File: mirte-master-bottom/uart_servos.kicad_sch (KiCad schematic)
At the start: 7 parts, among them J14 servo_connector, J17 servo_connector_small

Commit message: upd main layout v3
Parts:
- JP1: value LED_POWER_SELECT -> SERVO_POWER_SELECT
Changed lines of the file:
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@@
 			)
 		)
-		(property "Value" "LED_POWER_SELECT"
+		(property "Value" "SERVO_POWER_SELECT"
 			(at 76.2 91.44 90)
 			(effects

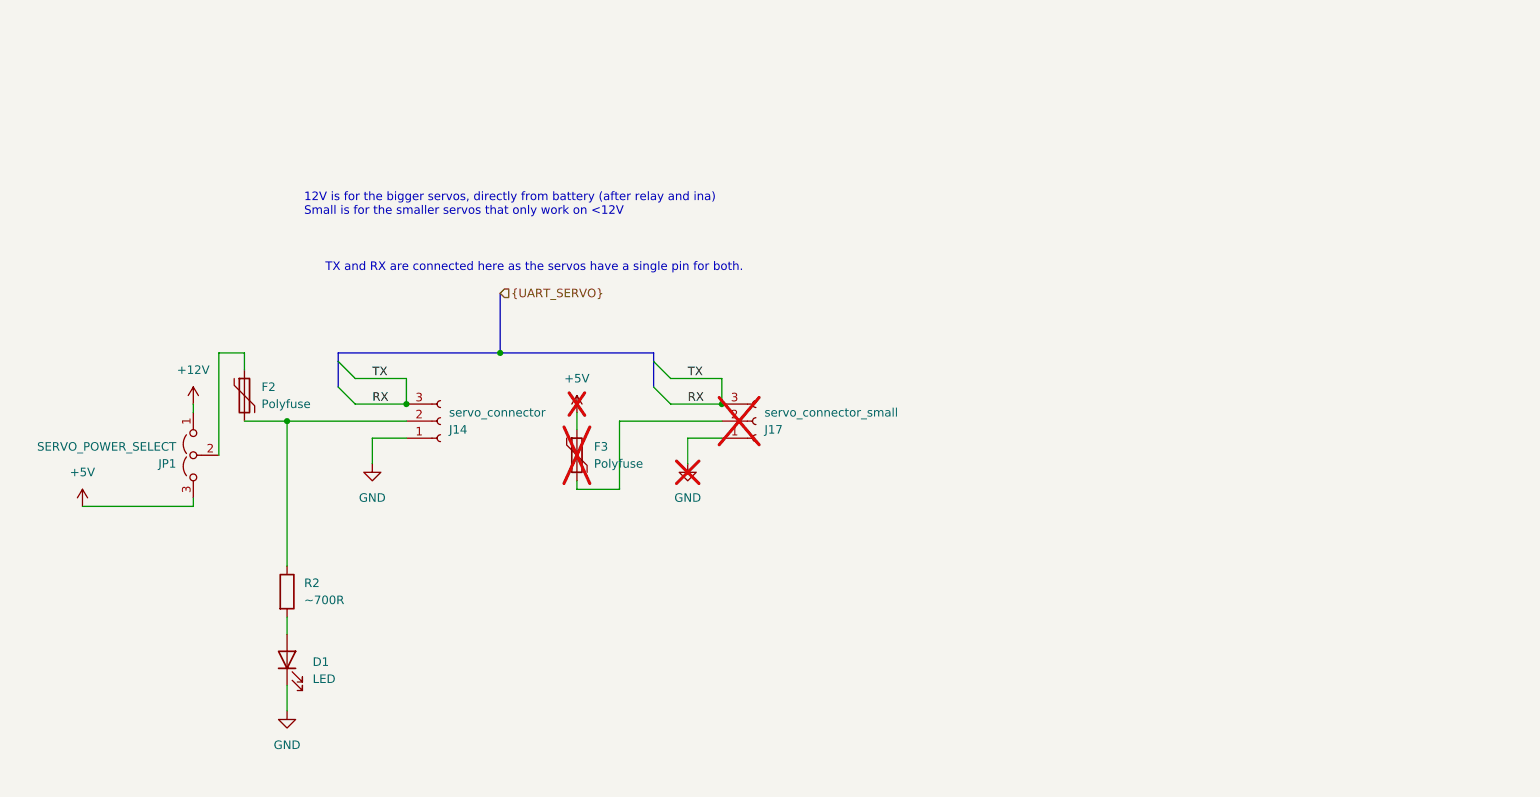
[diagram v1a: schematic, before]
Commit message: Upd power and hbridge, rm polyfuse
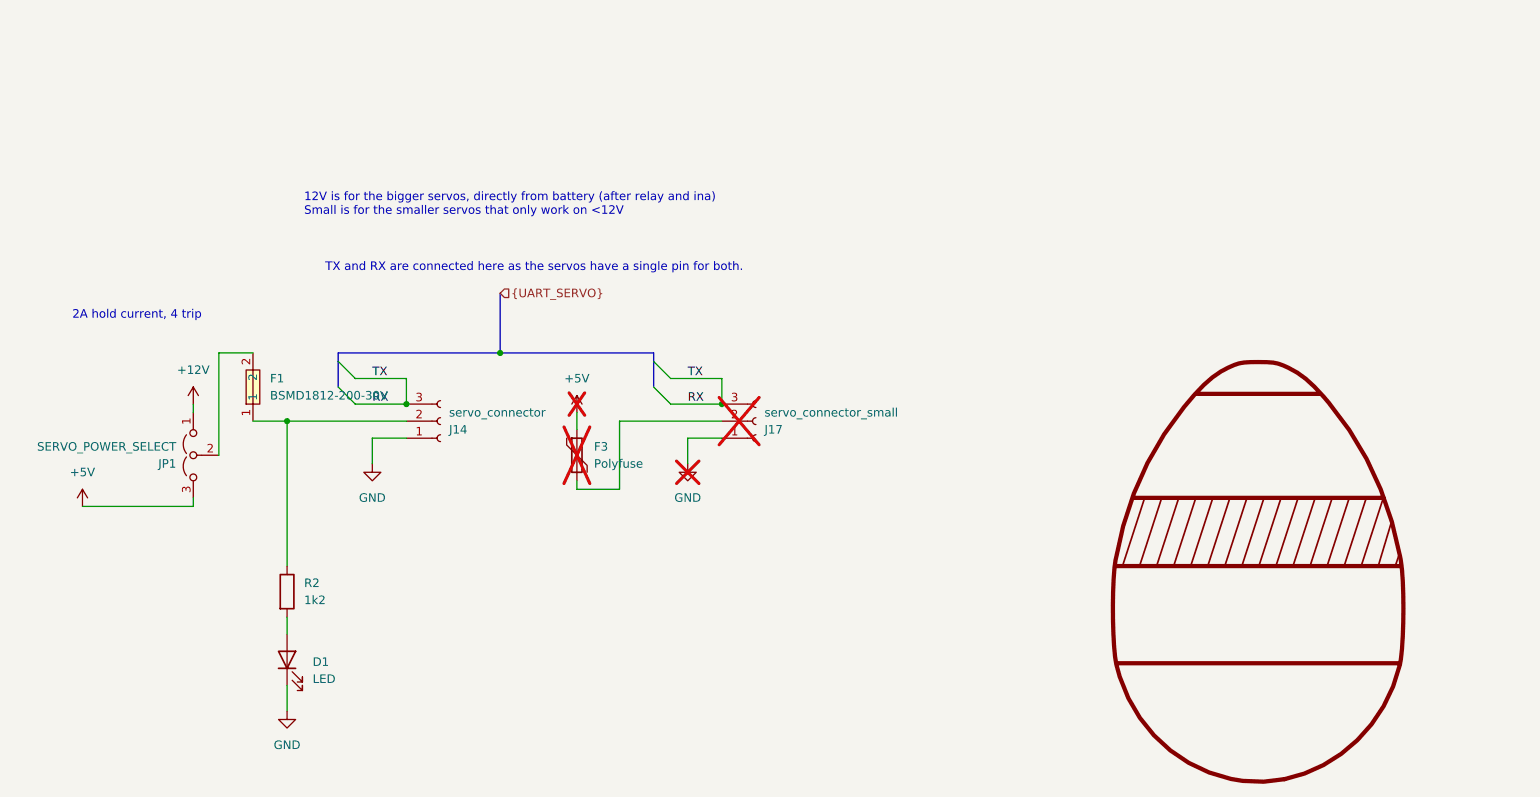
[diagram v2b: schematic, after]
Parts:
- removed F2: Polyfuse, Fuse:Fuse_1812_4532Metric, symbol Device:Polyfuse
- added F1: BSMD1812-200-30V, easyeda:F1812, symbol easyeda:BSMD1812-200-30V
- added SYM1: SYM_EasterEgg_42x60mm, Symbol:EasterEgg_EWG1308-2013_ClassA, symbol Graphic:SYM_EasterEgg_42x60mm
- R2: value ~700R -> 1k2
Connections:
- net at J14.2 (Pin_2), R2.1: now also F1.1
- net at JP1.2 (C): now also F1.2
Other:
- note added: "2A hold current, 4 trip"
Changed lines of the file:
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@@
 	(wire
 		(pts
-			(xy 82.55 77.47) (xy 86.36 77.47)
-		)
-		(stroke
-			(width 0)
-			(type default)
-		)
-	)
-	(wire
-		(pts
-			(xy 86.36 87.63) (xy 92.71 87.63)
+			(xy 82.55 77.47) (xy 87.63 77.47)
+		)
+		(stroke
+			(width 0)
+			(type default)
+		)
+	)
+	(wire
+		(pts
+			(xy 87.63 87.63) (xy 92.71 87.63)
 		)
 		(stroke
@@
 		(pts
 			(xy 147.32 77.47) (xy 147.32 78.74)
-		)
-		(stroke
-			(width 0)
-			(type default)
-		)
-	)
-	(wire
-		(pts
-			(xy 86.36 77.47) (xy 86.36 80.01)
 		)
 		(stroke
@@
 			)
 			(justify left bottom)
+		)
+	)
+	(text "2A hold current, 4 trip"
+		(exclude_from_sim no)
+		(at 70.358 71.882 0)
+		(effects
+			(font
+				(size 1.27 1.27)
+			)
 		)
 	)
@@
 			)
 		)
-		(property "Value" "~700R"
+		(property "Value" "1k2"
 			(at 95.25 114.2999 0)
 			(effects
@@
 				(path "/c479422a-501d-4123-8665-56a1c70bd9ea/2cdda85b-f21e-4225-a618-9cefba4ad079"
 					(reference "R2")
+					(unit 1)
+				)
+			)
+		)
+	)
+	(symbol
+		(lib_id "easyeda:BSMD1812-200-30V")
+		(at 87.63 82.55 90)
+		(unit 1)
+		(exclude_from_sim no)
+		(in_bom yes)
+		(on_board yes)
+		(dnp no)
+		(fields_autoplaced yes)
+		(property "Reference" "F1"
+			(at 90.17 81.2799 90)
+			(effects
+				(font
+					(size 1.27 1.27)
+				)
+				(justify right)
+			)
+		)
+		(property "Value" "BSMD1812-200-30V"
+			(at 90.17 83.8199 90)
+			(effects
+				(font
+					(size 1.27 1.27)
+				)
+				(justify right)
+			)
+		)
+		(property "Footprint" "easyeda:F1812"
+			(at 95.25 82.55 0)
+			(effects
+				(font
+					(size 1.27 1.27)
+				)
+				(hide yes)
+			)
+		)
+		(property "Datasheet" "https://lcsc.com/product-detail/PTC-Resettable-Fuses_BHFUSE-BSMD1812-200-30V_C960026.html"
+			(at 97.79 82.55 0)
+			(effects
+				(font
+					(size 1.27 1.27)
+				)
+				(hide yes)
+			)
+		)
+		(property "Description" ""
+			(at 87.63 82.55 0)
+			(effects
+				(font
+					(size 1.27 1.27)
+				)
+				(hide yes)
+			)
+		)
+		(property "LCSC Part" "C960026"
+			(at 100.33 82.55 0)
+			(effects
+				(font
+					(size 1.27 1.27)
+				)
+				(hide yes)
+			)
+		)
+		(pin "2"
+		)
+		(pin "1"
+		)
+		(instances
+			(project ""
+				(path "/c479422a-501d-4123-8665-56a1c70bd9ea/2cdda85b-f21e-4225-a618-9cefba4ad079"
+					(reference "F1")
 					(unit 1)
 				)
@@
 	)
 	(symbol
+		(lib_id "Graphic:SYM_EasterEgg_42x60mm")
+		(at 237.49 140.97 0)
+		(unit 1)
+		(exclude_from_sim no)
+		(in_bom no)
+		(on_board yes)
+		(dnp no)
+		(fields_autoplaced yes)
+		(property "Reference" "SYM1"
+			(at 237.49 140.97 0)
+			(effects
+				(font
+					(size 1.27 1.27)
+				)
+				(hide yes)
+			)
+		)
+		(property "Value" "SYM_EasterEgg_42x60mm"
+			(at 237.49 140.97 0)
+			(effects
+				(font
+					(size 1.27 1.27)
+				)
+				(hide yes)
+			)
+		)
+		(property "Footprint" "Symbol:EasterEgg_EWG1308-2013_ClassA"
+			(at 237.49 144.78 0)
+			(effects
+				(font
+					(size 1.27 1.27)
+				)
+				(hide yes)
+			)
+		)
+		(property "Datasheet" "https://eur-lex.europa.eu/LexUriServ/LexUriServ.do?uri=OJ:L:2013:347:0671:0854:de:PDF"
+			(at 237.49 147.32 0)
+			(effects
+				(font
+					(size 1.27 1.27)
+				)
+				(hide yes)
+			)
+		)
+		(property "Description" "EasterEgg, ClassA, Medium Size"
+			(at 237.49 140.97 0)
+			(effects
+				(font
+					(size 1.27 1.27)
+				)
+				(hide yes)
+			)
+		)
+		(property "Sim.Enable" "0"
+			(at 237.49 143.51 0)
+			(effects
+				(font
+					(size 1.27 1.27)
+				)
+				(hide yes)
+			)
+		)
+		(instances
+			(project ""
+				(path "/c479422a-501d-4123-8665-56a1c70bd9ea/2cdda85b-f21e-4225-a618-9cefba4ad079"
+					(reference "SYM1")
+					(unit 1)
+				)
+			)
+		)
+	)
+	(symbol
 		(lib_id "power:+5V")
 		(at 62.23 100.33 0)
@@
 					(unit 1)
 				)
-			)
-		)
-	)
-	(symbol
-		(lib_id "Device:Polyfuse")
-		(at 86.36 83.82 0)
-		(unit 1)
-		(exclude_from_sim no)
-		(in_bom yes)
-		(on_board yes)
-		(dnp no)
-		(fields_autoplaced yes)
-		(property "Reference" "F2"
-			(at 88.9 82.5499 0)
-			(effects
-				(font
-					(size 1.27 1.27)
-				)
-				(justify left)
-			)
-		)
-		(property "Value" "Polyfuse"
-			(at 88.9 85.0899 0)
-			(effects
-				(font
-					(size 1.27 1.27)
-				)
-				(justify left)
-			)
-		)
-		(property "Footprint" "Fuse:Fuse_1812_4532Metric"
-			(at 87.63 88.9 0)
-			(effects
-				(font
-					(size 1.27 1.27)
-				)
-				(justify left)
-				(hide yes)
-			)
-		)
-		(property "Datasheet" "~"
-			(at 86.36 83.82 0)
-			(effects
-				(font
-					(size 1.27 1.27)
-				)
-				(hide yes)
-			)
-		)
-		(property "Description" "Resettable fuse, polymeric positive temperature coefficient"
-			(at 86.36 83.82 0)
-			(effects
-				(font
-					(size 1.27 1.27)
-				)
-				(hide yes)
-			)
-		)
-		(pin "1"
-		)
-		(pin "2"
-		)
-		(instances
-			(project ""
-				(path "/c479422a-501d-4123-8665-56a1c70bd9ea/2cdda85b-f21e-4225-a618-9cefba4ad079"
-					(reference "F2")
-					(unit 1)
-				)

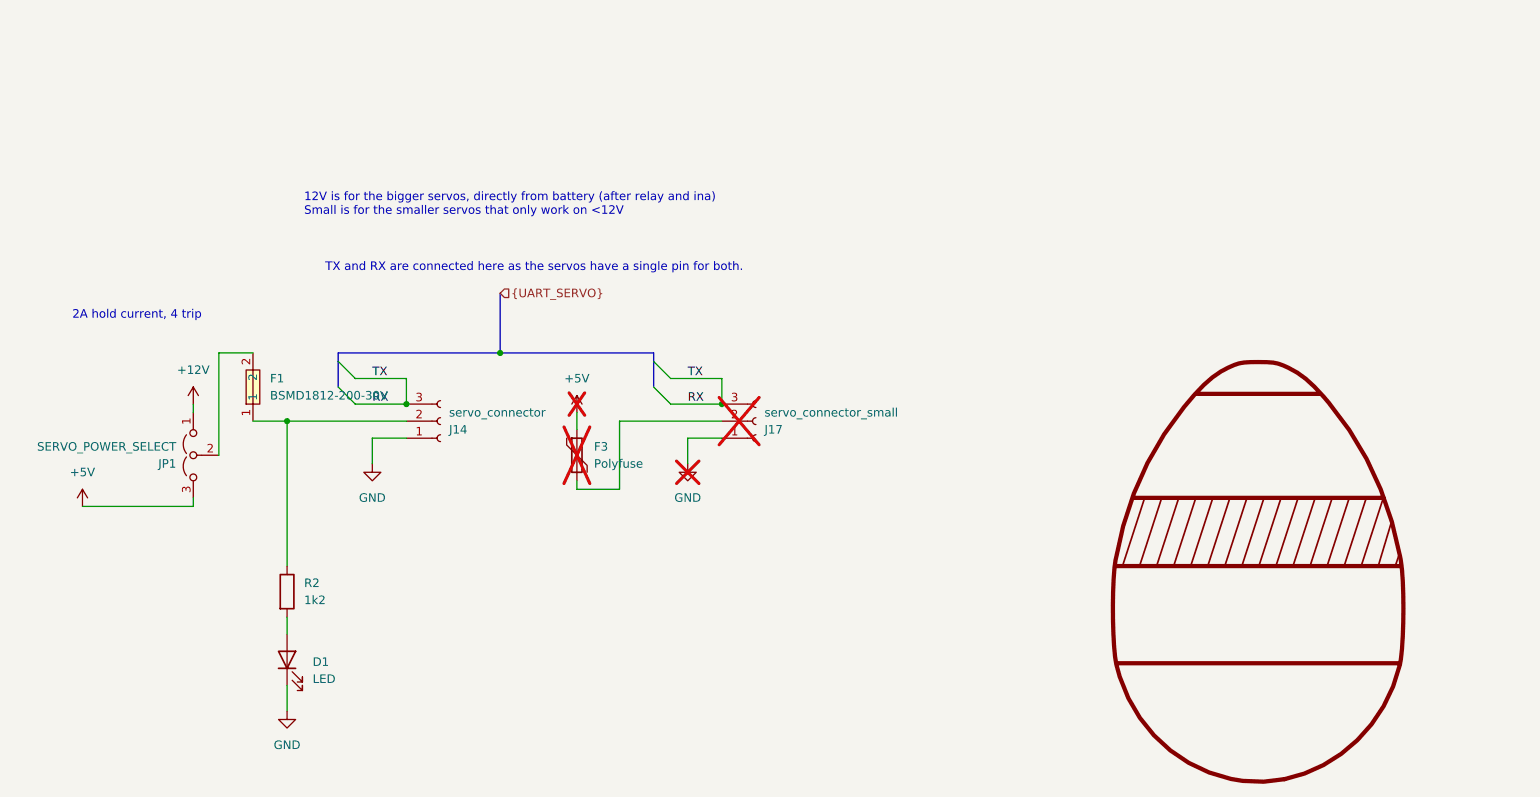
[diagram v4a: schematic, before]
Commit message: Add emergency switch by using mosfet for power
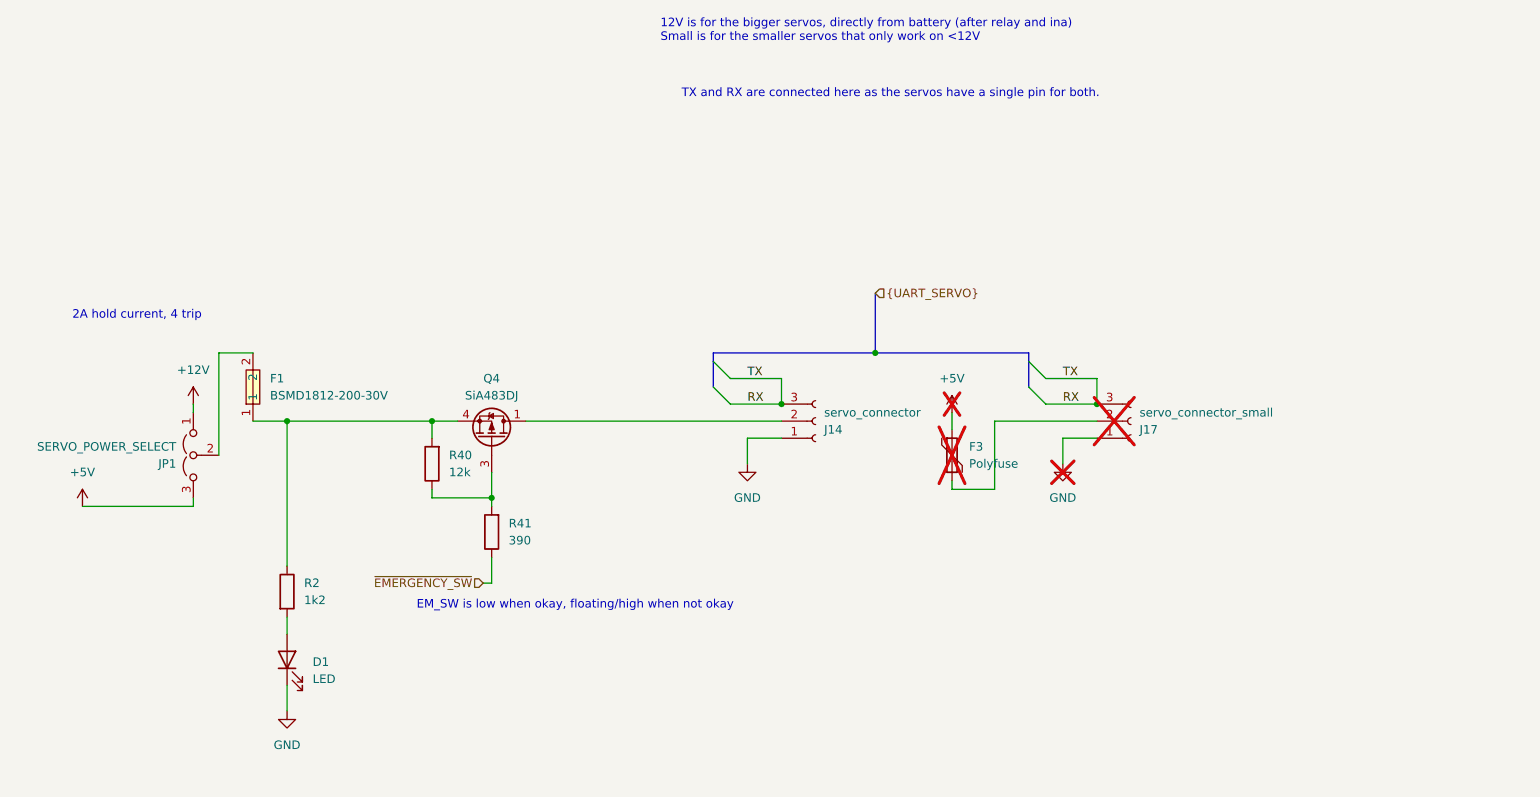
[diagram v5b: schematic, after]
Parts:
- removed SYM1: SYM_EasterEgg_42x60mm, Symbol:EasterEgg_EWG1308-2013_ClassA, symbol Graphic:SYM_EasterEgg_42x60mm
- added Q4: SiA483DJ, Package_TO_SOT_SMD:Vishay_PowerPAK_SC70-6L_Single, symbol Transistor_FET:SiA449DJ
- added R40: 12k, Resistor_SMD:R_0805_2012Metric, symbol Device:R
- added R41: 390, Resistor_SMD:R_0805_2012Metric, symbol Device:R
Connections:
- net at F1.1, R2.1: now also Q4.4 (S), R40.2; no longer J14.2 (Pin_2)
- new net: J14.2 (Pin_2), Q4.1 (D)
- new net: Q4.3 (G), R40.1, R41.2
- new net ~{EMERGENCY_SW}: R41.1
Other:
- note added: "EM_SW is low when okay, floating/high when not okay"
- moved on the sheet: F3, J14, J17

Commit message: change to 12v em switch
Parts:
- R41: value 390 -> 1k
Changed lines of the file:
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@@
 			)
 		)
-		(property "Value" "390"
+		(property "Value" "1k"
 			(at 125.73 105.4099 0)
 			(effects

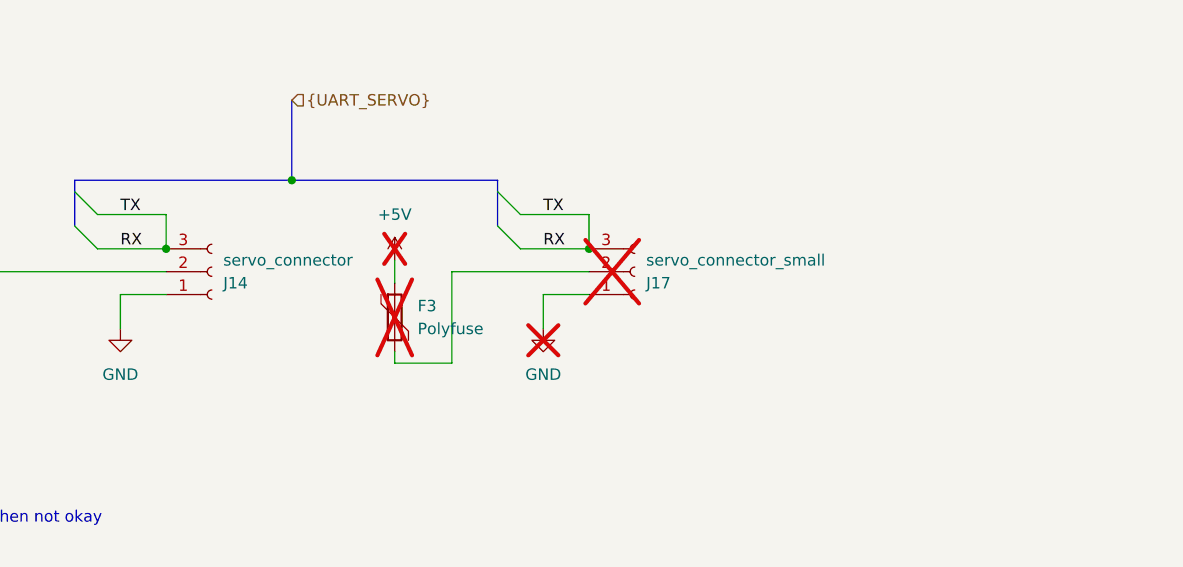
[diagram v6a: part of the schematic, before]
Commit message: Upd, add feetech servo connector
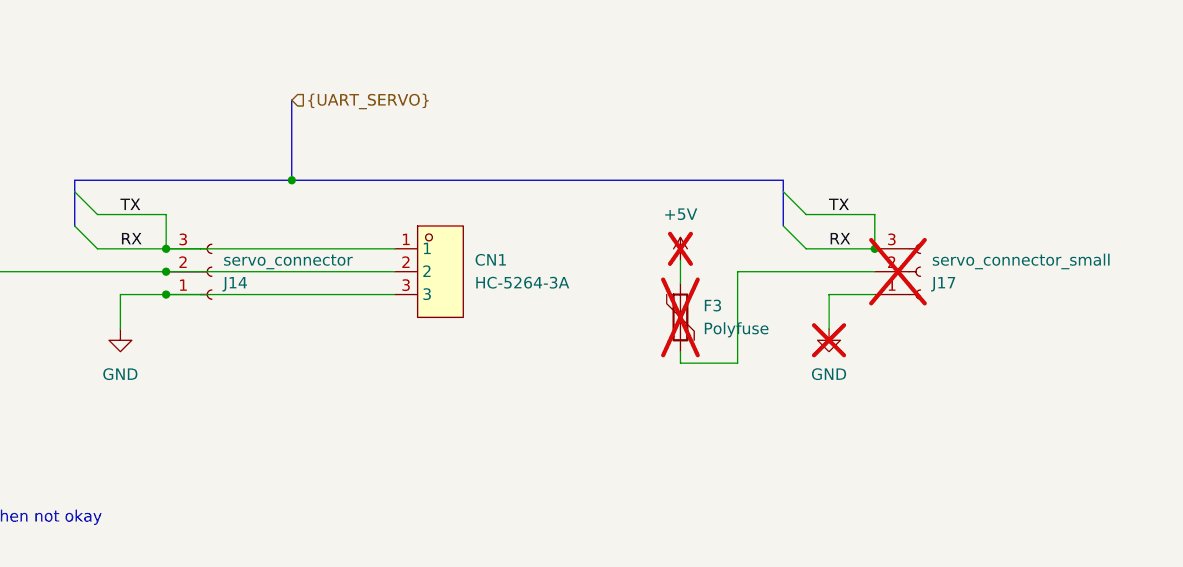
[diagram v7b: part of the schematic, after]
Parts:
- added CN1: HC-5264-3A, easyeda:CONN-TH_3P-P2.50_HCTL_HC-5264-3A, symbol easyeda:HC-5264-3A
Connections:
- net GND: now also CN1.3
- net RX: now also CN1.1
- net at J14.2 (Pin_2), Q4.1 (D): now also CN1.2
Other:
- moved on the sheet: F3, J17
